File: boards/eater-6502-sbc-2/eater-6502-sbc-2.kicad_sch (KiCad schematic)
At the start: 37 parts, among them J1 HDR_EXT_CLK, J2 HDR_CPU_BUS, J3 Jack-DC, J4 HDR_PA[0:4], SW1 SW_RESET, SW2 SW_SPDT, U1 W65C02SxP, U2 28C256, U3 KM62256CLP, U4 W65C22NxP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

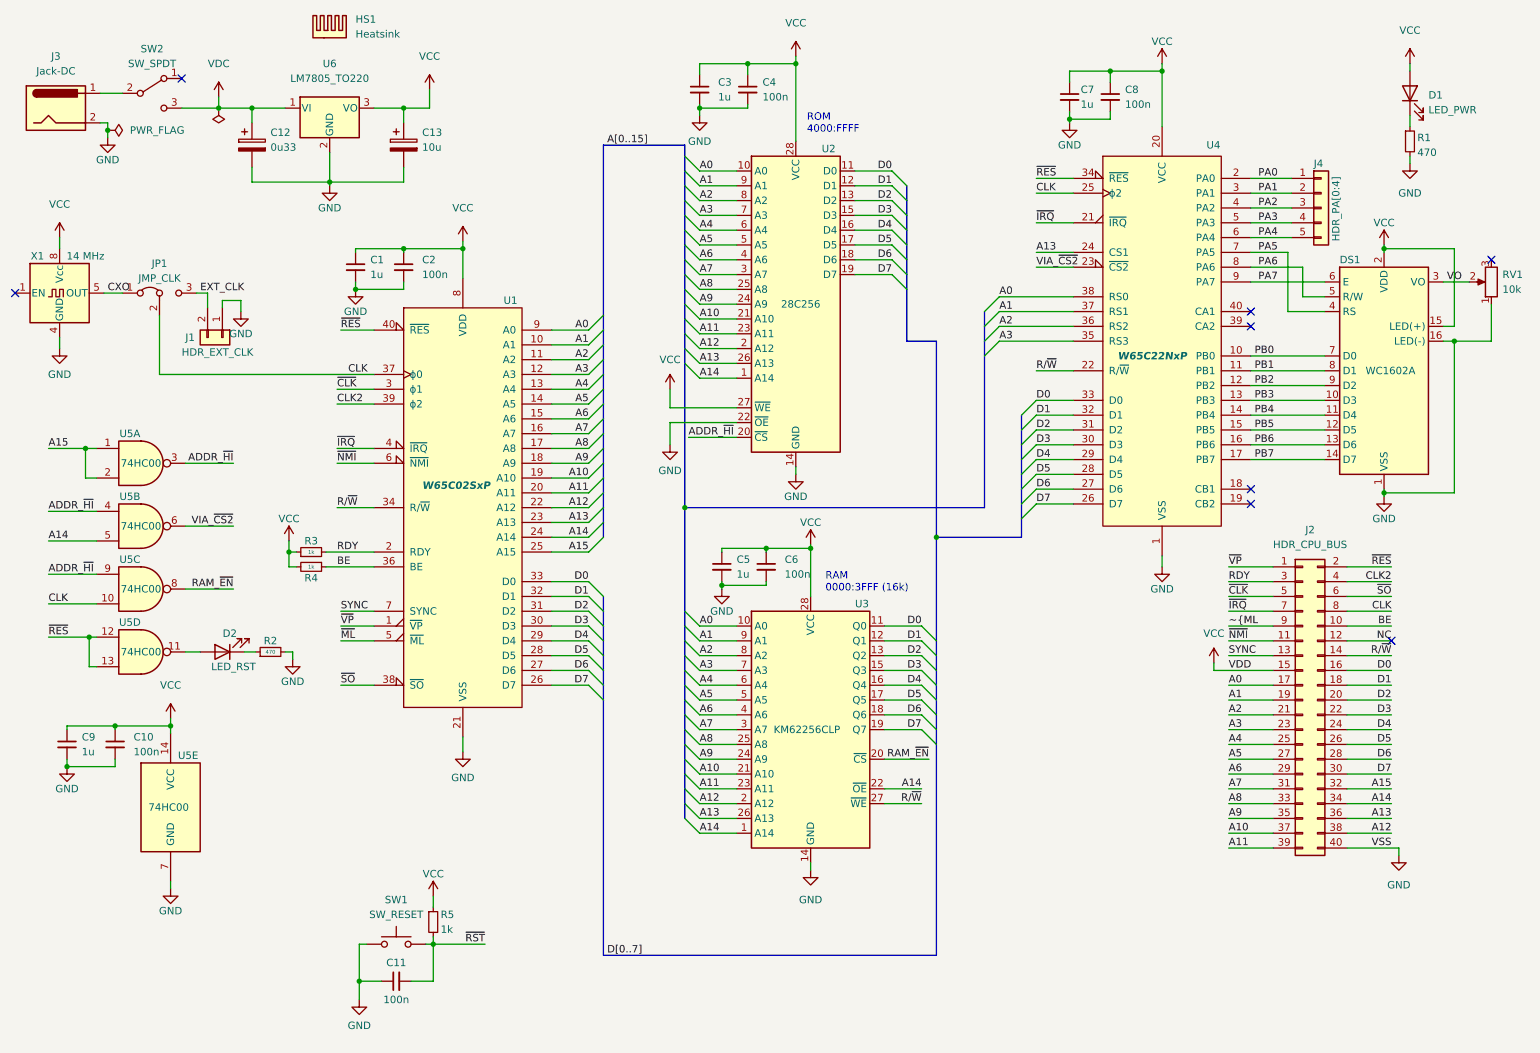
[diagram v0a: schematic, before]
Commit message: Finished rough layout and parts selection.
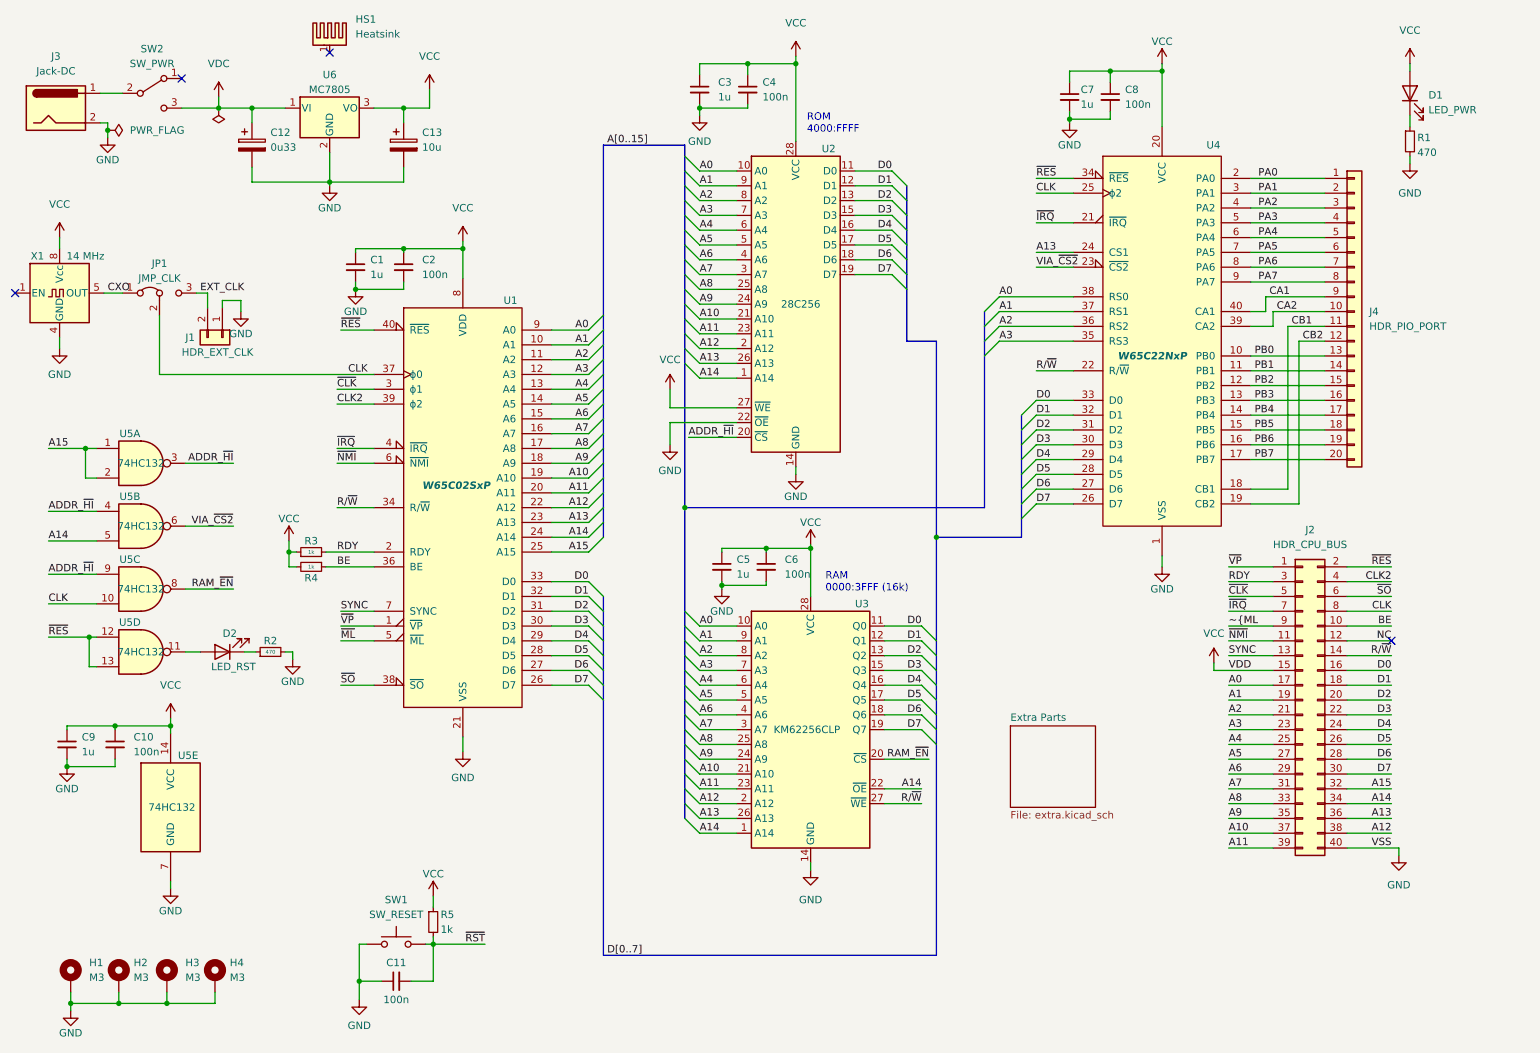
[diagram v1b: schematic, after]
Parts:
- removed DS1: WC1602A, Display:WC1602A, symbol Display_Character:WC1602A
- removed J4: HDR_PA[0:4], Connector_PinSocket_2.54mm:PinSocket_1x05_P2.54mm_Vertical, symbol Connector_Generic:Conn_01x05
- removed RV1: 10k, Potentiometer_THT:Potentiometer_Piher_PT-6-V_Vertical_Hole, symbol Device:R_Potentiometer
- added H1, H2, H3, H4: M3, MountingHole:MountingHole_3.2mm_M3_Pad, symbol Mechanical:MountingHole_Pad
- added J4: HDR_PIO_PORT, Connector_PinSocket_2.54mm:PinSocket_1x20_P2.54mm_Vertical, symbol Connector_Generic:Conn_01x20
- C1, C3, C5, C7, C9: footprint Capacitor_THT:C_Rect_L4.6mm_W5.5mm_P2.50mm_MKS02_FKP02 -> Capacitor_THT:C_Rect_L4.0mm_W2.5mm_P2.50mm; Manufacturer (none) -> TDK; Manufacturer Part Number (none) -> FG18X5R1H105KRT06; Supplier (none) -> Mouser; Supplier Part Number (none) -> 810-FG18X5R1H105KRT6
- C10, C11, C2, C4, C6, C8: Manufacturer (none) -> Vishay; Manufacturer Part Number (none) -> K104M15X7RF53L2; Supplier (none) -> Mouser; Supplier Part Number (none) -> 594-K104M15X7RF53L2
- C12: footprint Capacitor_THT:C_Rect_L4.6mm_W5.5mm_P2.50mm_MKS02_FKP02 -> Capacitor_THT:CP_Radial_D4.0mm_P1.50mm; Manufacturer (none) -> Rubycon; Manufacturer Part Number (none) -> 50NW50R33MEFC4X5; Supplier (none) -> Mouser; Supplier Part Number (none) -> 232-50NW50R33MEFC4X5
- C13: Manufacturer (none) -> Wurth Elektronik; Manufacturer Part Number (none) -> 860010572002; Supplier (none) -> Mouser; Supplier Part Number (none) -> 710-860010572002
- D1: Manufacturer (none) -> Wurth Elektronik; Manufacturer Part Number (none) -> 151051RS11000; Supplier (none) -> Mouser; Supplier Part Number (none) -> 710-151051RS11000
- D2: Manufacturer (none) -> Wurth Elektronik; Manufacturer Part Number (none) -> 151051BS04000; Supplier (none) -> Mouser; Supplier Part Number (none) -> 710-151051BS04000
- HS1: symbol Mechanical:Heatsink -> Mechanical:Heatsink_Pad; Manufacturer (none) -> Aavid; Manufacturer Part Number (none) -> 576802B03900G; Supplier (none) -> Mouser; Supplier Part Number (none) -> 532-576802B39G
- J1: Manufacturer (none) -> Preci-dip; Manufacturer Part Number (none) -> 801-87-002-20-001101; Supplier (none) -> Mouser; Supplier Part Number (none) -> 437-8018700220001101
- J2: Manufacturer (none) -> Wurth Elektronik; Manufacturer Part Number (none) -> 61304021821; Supplier (none) -> Mouser; Supplier Part Number (none) -> 710-61304021821
- J3: Manufacturer (none) -> CUI Devices; Manufacturer Part Number (none) -> PJ-063AH; Supplier (none) -> Mouser; Supplier Part Number (none) -> 490-PJ-063AH
- JP1: Manufacturer (none) -> Amphenol; Manufacturer Part Number (none) -> 10129378-920003BLF; Supplier (none) -> Mouser; Supplier Part Number (none) -> 649-1012937892003BLF
- R1, R2: Manufacturer (none) -> Vishay; Manufacturer Part Number (none) -> MBA02040C4700FRP00; Supplier (none) -> Mouser; Supplier Part Number (none) -> 594-5063JD470R0FT
- R3, R4, R5: Manufacturer (none) -> Vishay; Manufacturer Part Number (none) -> MBA02040C1001FRP00; Supplier (none) -> Mouser; Supplier Part Number (none) -> 594-5063JD1K000FT
- SW1: Manufacturer (none) -> CUI Devices; Manufacturer Part Number (none) -> TS02-66-43-BK-160-LCR-D; Supplier (none) -> Mouser; Supplier Part Number (none) -> 179-TS026643BK160LCR
- SW2: value SW_SPDT -> SW_PWR; footprint Button_Switch_THT:SW_Slide_1P2T_CK_OS102011MS2Q -> EaterLibrary:Button_Switch_SPST_NKK_CS12ANW03; Manufacturer (none) -> NKK Switches; Manufacturer Part Number (none) -> CS12ANW03; Supplier (none) -> Mouser; Supplier Part Number (none) -> 633-CS12ANW03
- U1: Manufacturer (none) -> WDC; Manufacturer Part Number (none) -> W65C02S6TPG-14; Supplier (none) -> Mouser; Supplier Part Number (none) -> 955-W65C02S6TPG-14
- U2: footprint Socket:DIP_Socket-28_W11.9_W12.7_W15.24_W17.78_W18.5_3M_228-1277-00-0602J -> Package_DIP:DIP-28_W15.24mm_Socket_LongPads; Manufacturer (none) -> Microchip; Manufacturer Part Number (none) -> AT28C256-15PU; Supplier (none) -> Mouser; Supplier Part Number (none) -> 556-AT28C25615PU
- U3: footprint Package_DIP:DIP-28_W15.24mm -> Package_DIP:DIP-28_W15.24mm_Socket_LongPads; Manufacturer (none) -> Alliance Memory; Manufacturer Part Number (none) -> AS6C62256-55PCN; Supplier (none) -> Mouser; Supplier Part Number (none) -> 913-AS6C62256-55PCN
- U4: Manufacturer (none) -> WDC; Manufacturer Part Number (none) -> W65C22S6TPG-14; Supplier (none) -> Mouser; Supplier Part Number (none) -> 955-W65C22S6TPG-14
- U5: value 74HC00 -> 74HC132; Manufacturer (none) -> Texas Instruments; Manufacturer Part Number (none) -> SN74HC132NE4; Supplier (none) -> Mouser; Supplier Part Number (none) -> 595-SN74HC132NE4
- U6: value LM7805_TO220 -> MC7805; Manufacturer (none) -> onsemi; Manufacturer Part Number (none) -> MC7805ACTG; Supplier (none) -> Mouser; Supplier Part Number (none) -> 863-MC7805ACTG
- X1: Manufacturer (none) -> Aries Electronics; Manufacturer Part Number (none) -> 1108800; Supplier (none) -> Mouser; Supplier Part Number (none) -> 535-1108800
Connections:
- net GND: now also H1.1, H2.1, H3.1, H4.1
- net PA0: now also J4.1 (Pin_1)
- net PA1: now also J4.2 (Pin_2)
- net PA2: now also J4.3 (Pin_3)
- net PA3: now also J4.4 (Pin_4)
- net PA4: now also J4.5 (Pin_5)
- net PA5: now also J4.6 (Pin_6)
- net PA6: now also J4.7 (Pin_7)
- net PA7: now also J4.8 (Pin_8)
- net PB0: now also J4.13 (Pin_13)
- net PB1: now also J4.14 (Pin_14)
- net PB2: now also J4.15 (Pin_15)
- net PB3: now also J4.16 (Pin_16)
- net PB4: now also J4.17 (Pin_17)
- net PB5: now also J4.18 (Pin_18)
- net PB6: now also J4.19 (Pin_19)
- net PB7: now also J4.20 (Pin_20)
- net CB1: now reaches U4.18 (CB1)
- net CB1: now also J4.11 (Pin_11)
- net CB2: now reaches U4.19 (CB2)
- net CB2: now also J4.12 (Pin_12)
- net CA2: now reaches U4.39 (CA2)
- net CA2: now also J4.10 (Pin_10)
- net CA1: now reaches U4.40 (CA1)
- net CA1: now also J4.9 (Pin_9)
- no-connect marks 8 -> 4
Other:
- added sheet Extra Parts (extra.kicad_sch)
